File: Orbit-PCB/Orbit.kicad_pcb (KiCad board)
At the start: 2 copper layers, 304.8 x 114.9 mm, 272 parts, among them J1 PJ-3200B-4A, J10 Breakaway_Tabs, J11 PJ-3200B-4A, J12 AVR-ISP-6, J13 Breakaway_Tabs, J14 Breakaway_Tabs, J15 Breakaway_Tabs, J16 Breakaway_Tabs, J17 Breakaway_Tabs, J18 Breakaway_Tabs, J19 Breakaway_Tabs, J2 AVR-ISP-6, J20 Breakaway_Tabs, J3 Breakaway_Tabs, J4 Breakaway_Tabs, J5 Breakaway_Tabs, J6 Breakaway_Tabs, J7 Breakaway_Tabs, J8 Breakaway_Tabs, J9 Breakaway_Tabs, Q1 2N7002, Q2 2N7002, SW1 SW_Push, SW2 SW_Push, U1 ATmega32U4-MU, U2 PRTR5V0U2X, U3 ATmega32U4-MU, U4 PRTR5V0U2X, Y1 16MHz, Y2 16MHz

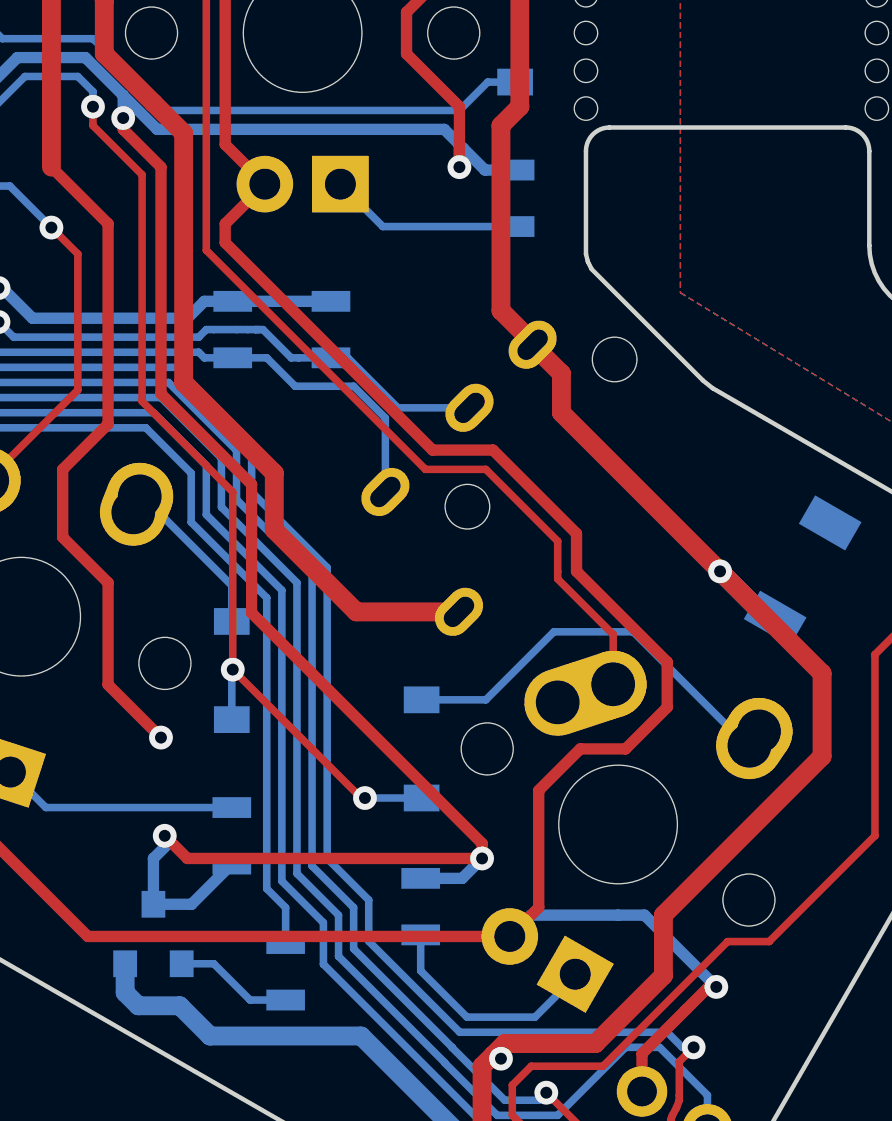
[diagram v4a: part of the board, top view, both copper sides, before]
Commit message: Clean a few more traces
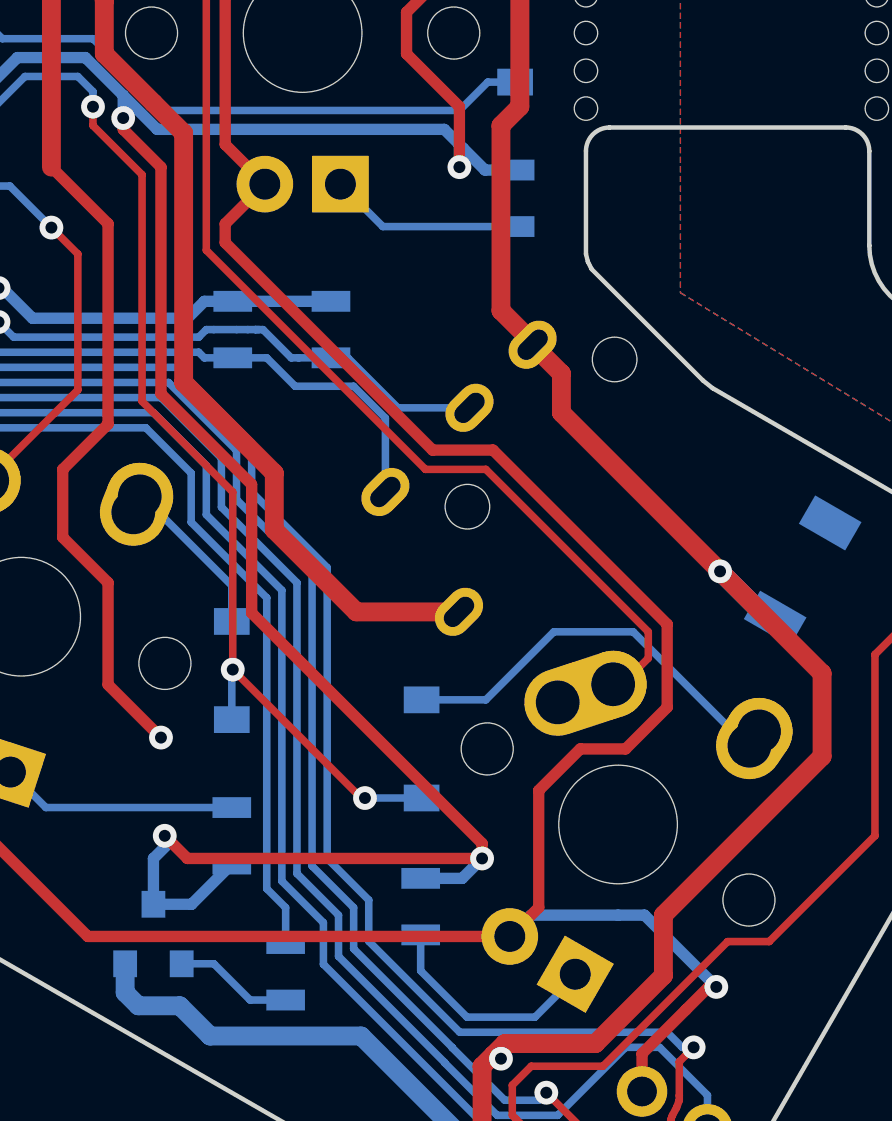
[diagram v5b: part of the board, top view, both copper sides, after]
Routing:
- net COL6: track 150.4 -> 153.7 mm
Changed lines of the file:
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@@
     (thickness 1.6)
     (drawings 204)
-    (tracks 3551)
+    (tracks 3548)
     (zones 0)
     (modules 272)
@@
   (segment (start 120.904 116.725) (end 119.519 116.725) (width 0.381) (layer B.Cu) (net 5))
   (segment (start 119.519 116.725) (end 119.507 116.713) (width 0.381) (layer B.Cu) (net 5))
-  (segment (start 161.925 125.476) (end 161.925 129.410557) (width 0.381) (layer F.Cu) (net 5))
-  (segment (start 164.846 124.079) (end 163.322 124.079) (width 0.381) (layer F.Cu) (net 5))
-  (segment (start 166.243 121.158) (end 166.243 122.682) (width 0.381) (layer F.Cu) (net 5))
-  (segment (start 163.195 118.11) (end 166.243 121.158) (width 0.381) (layer F.Cu) (net 5))
-  (segment (start 151.384 106.426) (end 151.384 107.061) (width 0.381) (layer F.Cu) (net 5))
-  (segment (start 163.322 124.079) (end 161.925 125.476) (width 0.381) (layer F.Cu) (net 5))
-  (segment (start 152.7175 105.0925) (end 151.384 106.426) (width 0.381) (layer F.Cu) (net 5))
-  (segment (start 151.384 107.061) (end 158.35629 114.03329) (width 0.381) (layer F.Cu) (net 5))
-  (segment (start 158.35629 114.03329) (end 160.38829 114.03329) (width 0.381) (layer F.Cu) (net 5))
-  (segment (start 161.925 129.410557) (end 160.952148 130.383409) (width 0.381) (layer F.Cu) (net 5))
-  (segment (start 166.243 122.682) (end 164.846 124.079) (width 0.381) (layer F.Cu) (net 5))
-  (segment (start 160.38829 114.03329) (end 163.195 116.84) (width 0.381) (layer F.Cu) (net 5))
-  (segment (start 163.195 116.84) (end 163.195 118.11) (width 0.381) (layer F.Cu) (net 5))
   (segment (start 159.244039 119.471652) (end 159.293348 119.471652) (width 0.635) (layer B.Cu) (net 5))
   (segment (start 147.32 98.933) (end 147.32 98.679) (width 0.635) (layer F.Cu) (net 5))
@@
   (segment (start 167.64 132.08) (end 166.878 132.842) (width 0.381) (layer F.Cu) (net 5))
   (segment (start 167.894 132.08) (end 167.64 132.08) (width 0.381) (layer F.Cu) (net 5))
+  (segment (start 158.35629 114.03329) (end 151.384 107.061) (width 0.381) (layer F.Cu) (net 5))
+  (segment (start 160.38829 114.03329) (end 158.35629 114.03329) (width 0.381) (layer F.Cu) (net 5))
+  (segment (start 166.243 119.888) (end 160.38829 114.03329) (width 0.381) (layer F.Cu) (net 5))
+  (segment (start 151.384 107.061) (end 151.384 106.426) (width 0.381) (layer F.Cu) (net 5))
+  (segment (start 160.952148 130.383409) (end 161.925 129.410557) (width 0.381) (layer F.Cu) (net 5))
+  (segment (start 161.925 129.410557) (end 161.925 125.476) (width 0.381) (layer F.Cu) (net 5))
+  (segment (start 161.925 125.476) (end 163.322 124.079) (width 0.381) (layer F.Cu) (net 5))
+  (segment (start 163.322 124.079) (end 164.846 124.079) (width 0.381) (layer F.Cu) (net 5))
+  (segment (start 151.384 106.426) (end 152.7175 105.0925) (width 0.381) (layer F.Cu) (net 5))
+  (segment (start 164.846 124.079) (end 166.243 122.682) (width 0.381) (layer F.Cu) (net 5))
+  (segment (start 166.243 122.682) (end 166.243 119.888) (width 0.381) (layer F.Cu) (net 5))
   (segment (start 48.29275 51.65625) (end 46.83125 51.65625) (width 0.254) (layer B.Cu) (net 6))
   (segment (start 52.197 47.752) (end 48.29275 51.65625) (width 0.254) (layer B.Cu) (net 6))
@@
   (segment (start 150.749 96.901) (end 150.749 78.994) (width 0.254) (layer F.Cu) (net 62))
   (segment (start 150.1775 97.4725) (end 150.749 96.901) (width 0.254) (layer F.Cu) (net 62))
-  (segment (start 160.147 114.681) (end 162.562443 117.096443) (width 0.254) (layer F.Cu) (net 62))
-  (segment (start 158.115 114.681) (end 160.147 114.681) (width 0.254) (layer F.Cu) (net 62))
-  (segment (start 150.749 107.315) (end 158.115 114.681) (width 0.254) (layer F.Cu) (net 62))
-  (segment (start 150.1775 97.4725) (end 150.749 98.044) (width 0.254) (layer F.Cu) (net 62))
-  (segment (start 150.749 98.044) (end 150.749 107.315) (width 0.254) (layer F.Cu) (net 62))
-  (segment (start 162.562443 118.11) (end 162.562443 118.366443) (width 0.254) (layer F.Cu) (net 62))
-  (segment (start 162.562443 117.096443) (end 162.562443 118.11) (width 0.254) (layer F.Cu) (net 62))
-  (segment (start 164.426936 120.230936) (end 164.426936 121.904898) (width 0.254) (layer F.Cu) (net 62))
-  (segment (start 162.562443 118.366443) (end 164.426936 120.230936) (width 0.254) (layer F.Cu) (net 62))
   (segment (start 124.362 113.395) (end 122.158 113.395) (width 0.254) (layer B.Cu) (net 62))
   (segment (start 122.158 113.395) (end 121.412 112.649) (width 0.254) (layer B.Cu) (net 62))
@@
   (segment (start 120.015 111.887) (end 120.015 111.379) (width 0.254) (layer F.Cu) (net 62))
   (segment (start 120.015 111.379) (end 120.523 110.871) (width 0.254) (layer F.Cu) (net 62))
+  (segment (start 164.124705 122.514295) (end 162.562443 122.514295) (width 0.254) (layer F.Cu) (net 62))
+  (segment (start 165.608 121.031) (end 164.124705 122.514295) (width 0.254) (layer F.Cu) (net 62))
+  (segment (start 150.749 98.044) (end 150.749 107.315) (width 0.254) (layer F.Cu) (net 62))
+  (segment (start 150.1775 97.4725) (end 150.749 98.044) (width 0.254) (layer F.Cu) (net 62))
+  (segment (start 150.749 107.315) (end 158.115 114.681) (width 0.254) (layer F.Cu) (net 62))
+  (segment (start 158.115 114.681) (end 160.147 114.681) (width 0.254) (layer F.Cu) (net 62))
+  (segment (start 160.147 114.681) (end 165.608 120.142) (width 0.254) (layer F.Cu) (net 62))
+  (segment (start 165.608 120.142) (end 165.608 121.031) (width 0.254) (layer F.Cu) (net 62))
   (segment (start 42.38375 75.5625) (end 40.9575 74.13625) (width 0.254) (layer B.Cu) (net 63))
   (segment (start 46.83125 75.5625) (end 42.38375 75.5625) (width 0.254) (layer B.Cu) (net 63))

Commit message: Add left/right hand detection pullup/downs
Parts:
- added G***: LOGO, locallib:icon-4.8, B.Cu at (33.3, 120.7)
- added G***: LOGO, locallib:ai-4.8-mask, F.Cu at (47.6, 117.5)
- added G***: LOGO, locallib:ai-4.8-mask, F.Cu at (317.5, 117.5)
- added G***: LOGO, locallib:icon-4.8, B.Cu at (331.8, 120.7)
- added J21: Conn_01x01, Mounting_Holes:MountingHole_3.5mm_Pad_Via, F.Cu at (177.0, 34.9)
- added MH1: HOLE, Mounting_Holes:MountingHole_5mm, F.Cu at (106.4, 69.1)
- added MH2: HOLE, Mounting_Holes:MountingHole_5mm, F.Cu at (258.8, 69.1)
- added R87: 10k, Resistors_SMD:R_0805, B.Cu at (120.9, 121.4)
- added R88: 10k, Resistors_SMD:R_0805, B.Cu at (243.3, 106.8)
- added REF**: 1U, MX_Alps_Hybrid:MX-1U, F.Cu at (182.6, 81.0)
- added REF**: 1U, MX_Alps_Hybrid:MX-1U, F.Cu at (182.6, 100.0)
- moved J20 135.5 mm to (325.4, 123.8), turned to 0 degrees
- moved J6 126.3 mm to (39.7, 123.8), turned to 0 degrees
- moved J19 96.0 mm to (268.3, 31.0), turned to 180 degrees
- moved J9 91.1 mm to (96.8, 31.0), turned to 180 degrees
- moved J18 71.4 mm to (249.2, 123.8), turned to 0 degrees
- moved J10 61.9 mm to (115.9, 123.8), turned to 0 degrees
- moved J17 59.2 mm to (233.4, 31.0), turned to 180 degrees
- moved J5 58.8 mm to (132.6, 31.0), turned to 180 degrees
- moved J15 28.6 mm to (201.6, 90.5)
- moved J16 28.6 mm to (192.1, 90.5)
- moved J4 28.6 mm to (163.5, 90.5)
- moved J8 28.6 mm to (173.0, 90.5)
- moved J13 7.14 mm to (201.6, 50.0)
- moved J14 7.14 mm to (192.1, 50.0)
- moved J3 7.14 mm to (163.5, 50.0)
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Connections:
- U1 pad 22: Net-(U1-Pad22) -> HDETECT
- U3 pad 22: Net-(U3-Pad22) -> HDETECT-R
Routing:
- net GND: track 1078.4 -> 1101.4 mm, vias 20 -> 21
- net GNDA: track 803.1 -> 814.4 mm
- net +5V: track 1001.8 -> 1009.2 mm, vias 9 -> 10
- net HDETECT-R: track 0.00 -> 7.32 mm
- net HDETECT: track 0.00 -> 7.07 mm
- net SDA: track 48.1 -> 44.4 mm
- net SCL: track 45.9 -> 43.5 mm
- net SCL-R: track 47.7 -> 45.8 mm
- net SDA-R: track 44.9 -> 43.1 mm
- net Net-(MX11-Pad4): track 6.46 -> 5.67 mm
- net COL1: track 153.2 -> 153.9 mm
- net Net-(D35-Pad2): track 9.86 -> 10.5 mm
- added copper zone on B.Cu, net GNDS
- added copper zone on F.Cu, net GNDS
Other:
- board size 304.8 x 114.9 mm -> 304.8 x 145.3 mm
- board text added: "Orbit PCB Rev 1.1 by ai03"

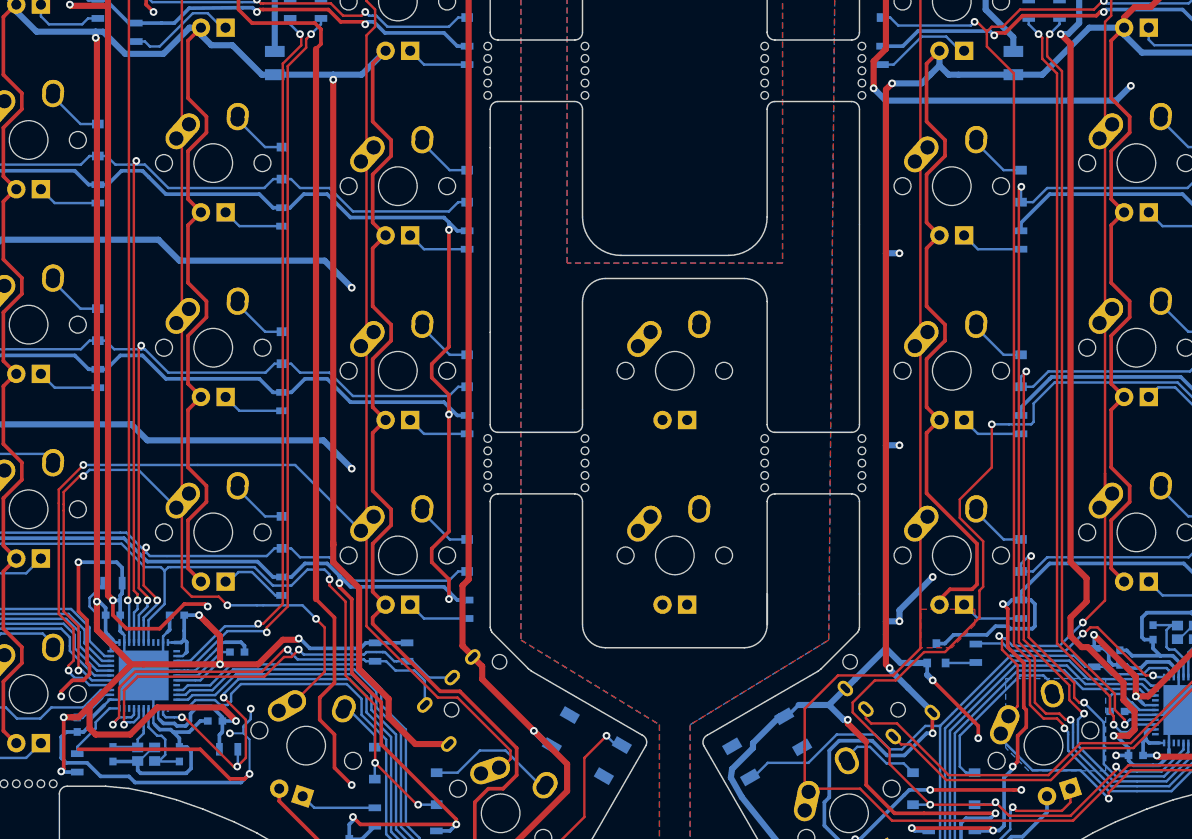
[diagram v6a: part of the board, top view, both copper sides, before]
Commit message: Clean a few tracks
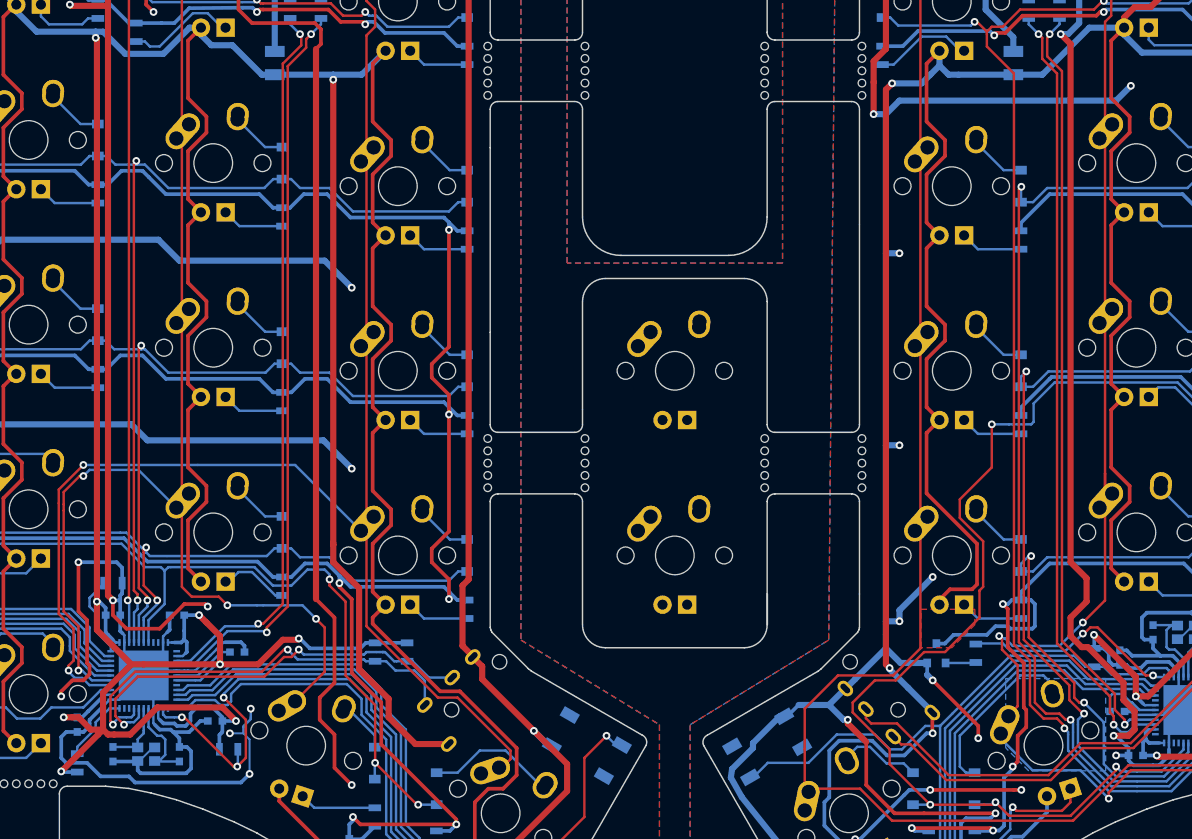
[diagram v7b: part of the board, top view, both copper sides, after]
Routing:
- net GND: track 1101.4 -> 1082.2 mm
- net GNDA: track 814.4 -> 815.7 mm
- net SCL: track 43.5 -> 44.2 mm
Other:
- net class POWER: trace_width 0.381 -> 0.635

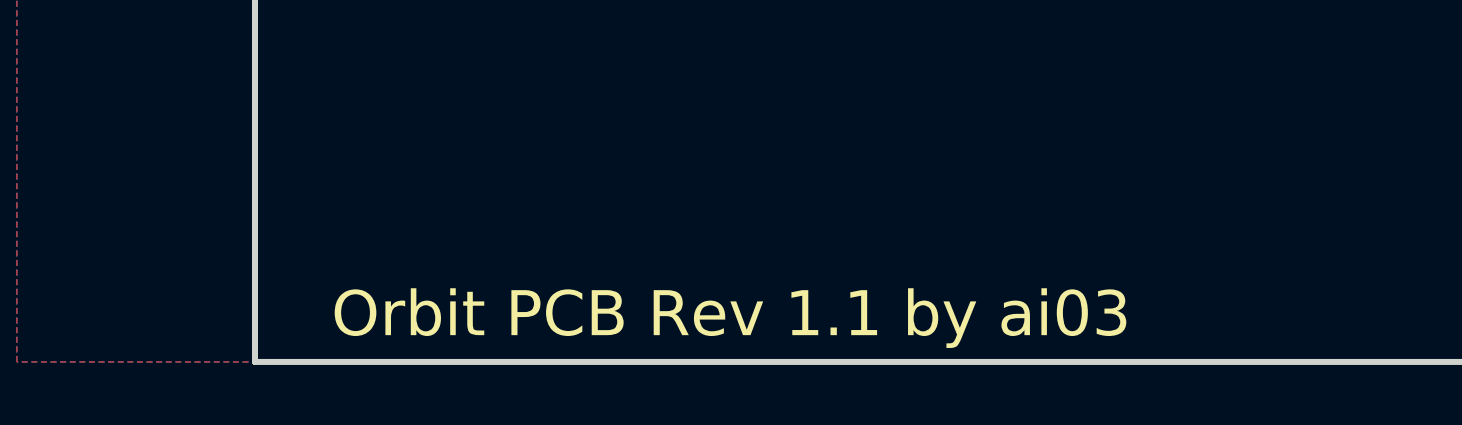
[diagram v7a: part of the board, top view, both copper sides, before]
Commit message: Wrong versioning
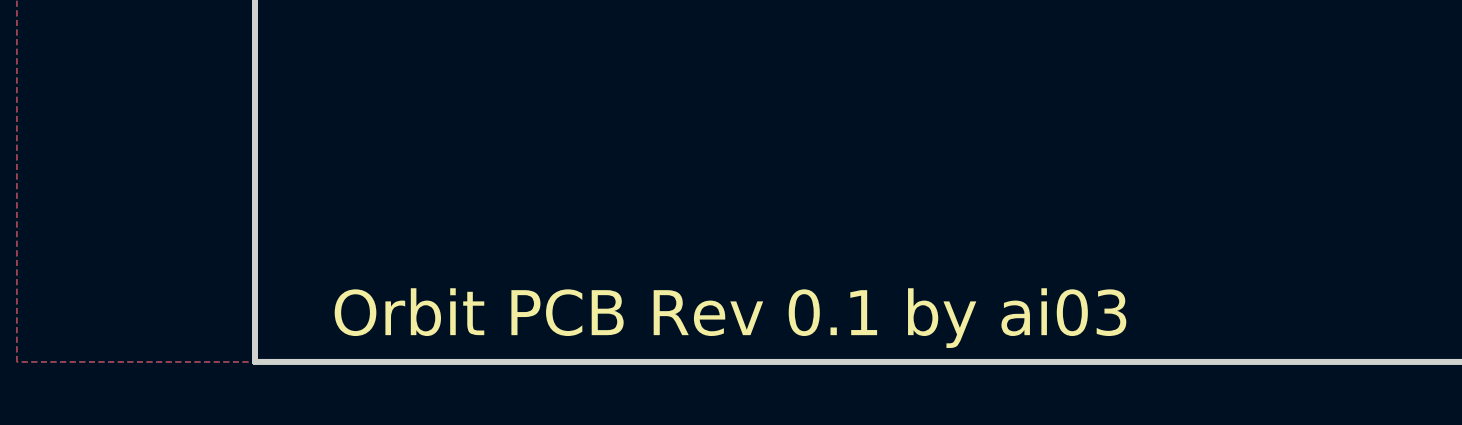
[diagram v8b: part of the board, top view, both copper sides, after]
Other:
- board text added: "Orbit PCB Rev 0.1 by ai03"
- board text removed: "Orbit PCB Rev 1.1 by ai03"
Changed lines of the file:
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@@
   (gr_line (start 210.2485 116.2685) (end 205.9305 120.5865) (layer B.SilkS) (width 0.2))
   (gr_line (start 201.676 107.696) (end 210.2485 116.2685) (layer B.SilkS) (width 0.2))
-  (gr_text "Orbit PCB Rev 1.1 by ai03" (at 47.625 157.1625) (layer F.SilkS)
+  (gr_text "Orbit PCB Rev 0.1 by ai03" (at 47.625 157.1625) (layer F.SilkS)
     (effects (font (size 1.5 1.5) (thickness 0.3)))
   )
